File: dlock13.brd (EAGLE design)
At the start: 100 x 80 mm, 18 parts, among them IC2 7805T, Q1 IRLZ44Z, Q2 IRLZ44Z

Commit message: Updated.
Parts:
- removed R12: 4.7k, rcl:0207/10
- R5: value 470 -> 4.7k
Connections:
- removed net N$6: Q2.S, R12.2
- net GND: now also Q2.S; no longer R12.1
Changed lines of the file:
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@@
 <element name="R10" library="resistor" package="0204/7" value="470" x="29.23" y="41.34" rot="MR90"/>
 <element name="Q2" library="transistor-power" package="TO220BH" value="IRLZ44Z" x="23.89" y="31.02" rot="MR270"/>
-<element name="R5" library="resistor" package="0204/7" value="470" x="32.77" y="40.82" rot="MR270"/>
-<element name="R12" library="rcl" package="0207/10" value="4.7k" x="67.25" y="20.23" rot="MR0"/>
+<element name="R5" library="resistor" package="0204/7" value="4.7k" x="32.77" y="40.82" rot="MR270"/>
 <element name="D4" library="diode" package="DO41-10" value="1N4004" x="39.25" y="17.8" rot="MR0"/>
 <element name="JP1" library="pinhead" package="1X02" value="" x="26.66" y="4.53" rot="MR0"/>
@@
 <contactref element="C2" pad="2"/>
 <contactref element="C1" pad="2"/>
-<contactref element="R12" pad="1"/>
 <contactref element="JP1" pad="2"/>
 <contactref element="JP2" pad="2"/>
@@
 <contactref element="J3" pad="2"/>
 <contactref element="Q1" pad="S"/>
-<wire x1="5.06" y1="32.95" x2="27.86" y2="17.99" width="0" layer="19" extent="1-1"/>
-<wire x1="27.22" y1="68.24" x2="5.06" y2="32.95" width="0" layer="19" extent="1-1"/>
-<wire x1="7.97" y1="6.43" x2="5.06" y2="32.95" width="0" layer="19" extent="1-1"/>
-<wire x1="12.77" y1="3.43" x2="7.97" y2="6.43" width="0" layer="19" extent="1-1"/>
-<wire x1="72.33" y1="20.23" x2="27.86" y2="17.99" width="0" layer="19" extent="1-1"/>
-<wire x1="25.39" y1="4.53" x2="72.33" y2="20.23" width="0" layer="19" extent="1-1"/>
+<contactref element="Q2" pad="S"/>
+<wire x1="38.88" y1="40.61" x2="27.22" y2="68.24" width="0" layer="19" extent="1-1"/>
+<wire x1="30.24" y1="28.48" x2="38.88" y2="40.61" width="0" layer="19" extent="1-1"/>
+<wire x1="27.86" y1="17.99" x2="30.24" y2="28.48" width="0" layer="19" extent="1-1"/>
+<wire x1="35.36" y1="7.74" x2="27.86" y2="17.99" width="0" layer="19" extent="1-1"/>
+<wire x1="42.39" y1="7.64" x2="35.36" y2="7.74" width="0" layer="19" extent="1-1"/>
+<wire x1="25.39" y1="4.53" x2="35.36" y2="7.74" width="0" layer="19" extent="1-1"/>
 <wire x1="19.04" y1="4.53" x2="25.39" y2="4.53" width="0" layer="19" extent="1-1"/>
-<wire x1="42.39" y1="7.64" x2="25.39" y2="4.53" width="0" layer="19" extent="1-1"/>
-<wire x1="35.36" y1="7.74" x2="42.39" y2="7.64" width="0" layer="19" extent="1-1"/>
-<wire x1="38.88" y1="40.61" x2="19.04" y2="4.53" width="0" layer="19" extent="1-1"/>
+<wire x1="12.77" y1="3.43" x2="19.04" y2="4.53" width="0" layer="19" extent="1-1"/>
+<wire x1="7.97" y1="6.43" x2="12.77" y2="3.43" width="0" layer="19" extent="1-1"/>
+<wire x1="5.06" y1="32.95" x2="30.24" y2="28.48" width="0" layer="19" extent="1-1"/>
 </signal>
 <signal name="VCC">
@@
 <wire x1="29.23" y1="45.15" x2="22.14" y2="68.24" width="0" layer="19" extent="1-1"/>
 </signal>
-<signal name="N$6">
-<contactref element="R12" pad="2"/>
-<contactref element="Q2" pad="S"/>
-<wire x1="30.24" y1="28.48" x2="62.17" y2="20.23" width="0" layer="19" extent="1-1"/>
-</signal>
 <signal name="N$7">

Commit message: Add vidarkr's changes. Produced and In use.
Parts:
- removed SV1: (no value), con-ml:ML26
- added C3: (no value), rcl:E1,8-4
- added D1: 1N4004DO41-10LARGEPADS, diode:DO41-10
- added PICONNECTOR: RASPBERRY-PI, RaspberryPi:RASPBERRY-PI_REV1
- D4: value 1N4004 -> 1N4004DO41-10LARGEPADS
- R10, R5: device resistor:0204/7 -> rcl:0207/10
- moved R2 50.3 mm to (22.9, 20.3), flipped to the top, turned to 90 degrees
- moved LED1 47.0 mm to (68.6, 20.3), flipped to the top, turned to 90 degrees
- moved SV2 43.8 mm to (3.81, 35.6), flipped to the top
- moved Q1 40.6 mm to (56.0, 36.0), flipped to the top, turned to 0 degrees
- moved R1 39.5 mm to (26.7, 20.3), flipped to the top, turned to 90 degrees
- moved C2 36.7 mm to (2.54, 25.4), flipped to the top
- moved R3 32.9 mm to (64.8, 25.4), flipped to the top, turned to 0 degrees
- moved D4 25.1 mm to (20.3, 34.3), flipped to the top, turned to 90 degrees
- moved R10 22.9 mm to (45.7, 25.4), flipped to the top, turned to 0 degrees
- moved C1 22.8 mm to (43.2, 30.5), flipped to the top, turned to 90 degrees
- moved IC2 18.6 mm to (13.0, 36.0), flipped to the top, turned to 0 degrees
- moved Q2 14.3 mm to (35.6, 39.4), flipped to the top
- moved JP2 10.8 mm to (19.1, 15.2), flipped to the top, turned to 180 degrees
- moved JP1 9.37 mm to (20.3, 11.4), flipped to the top, turned to 180 degrees
- moved R5 8.64 mm to (24.1, 40.6), flipped to the top, turned to 90 degrees
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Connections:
- removed net N$1: R5.1, SV1.22
- removed net N$12: JP2.1, SV1.15
- removed net N$8: JP1.1, R1.1, SV1.16
- removed net N$9: LED1.A, SV1.26
- new net GPI10_OUTERDOOR: PICONNECTOR.19, R5.1
- new net GPIO11_INNERDOOR: PICONNECTOR.23, R10.1
- new net GPIO17_J1: JP1.1, PICONNECTOR.11, R1.1
- new net GPIO22_J2: JP2.1, PICONNECTOR.15, R2.1
- net +12V: now also D1.C
- net +3V3: now also PICONNECTOR.1; no longer SV1.1
- net GND: now also C3.-, PICONNECTOR.25, PICONNECTOR.9; no longer SV1.25
- net N$13: now also LED1.A, PICONNECTOR.26; no longer Q1.D, SV2.1
- net N$2: now also D1.A, Q1.D, SV2.1; no longer R10.1, SV1.18
- net VCC: now also C3.+, PICONNECTOR.2, PICONNECTOR.4; no longer SV1.2
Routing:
- net VCC: track 0.00 -> 88.2 mm, vias 0 -> 6
- net N$2: track 0.00 -> 77.9 mm
- net +12V: track 0.00 -> 55.9 mm
- net N$13: track 0.00 -> 51.0 mm
- net +3V3: track 0.00 -> 44.5 mm, vias 0 -> 2
- net GPI10_OUTERDOOR: track 0.00 -> 38.2 mm
- net GPIO22_J2: track 0.00 -> 35.0 mm
- net N$14: track 0.00 -> 29.0 mm
- net GPIO11_INNERDOOR: track 0.00 -> 27.2 mm
- net GPIO17_J1: track 0.00 -> 18.6 mm
- net N$7: track 0.00 -> 6.35 mm
- net N$4: track 0.00 -> 5.70 mm
- net N$11: track 0.00 -> 4.34 mm
- net N$15: track 0.00 -> 2.84 mm
- net N$9: track 0.00 -> 2.00 mm
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- added copper zone on layer 16, net GND
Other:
- board size 100 x 80 mm -> 72 x 51 mm

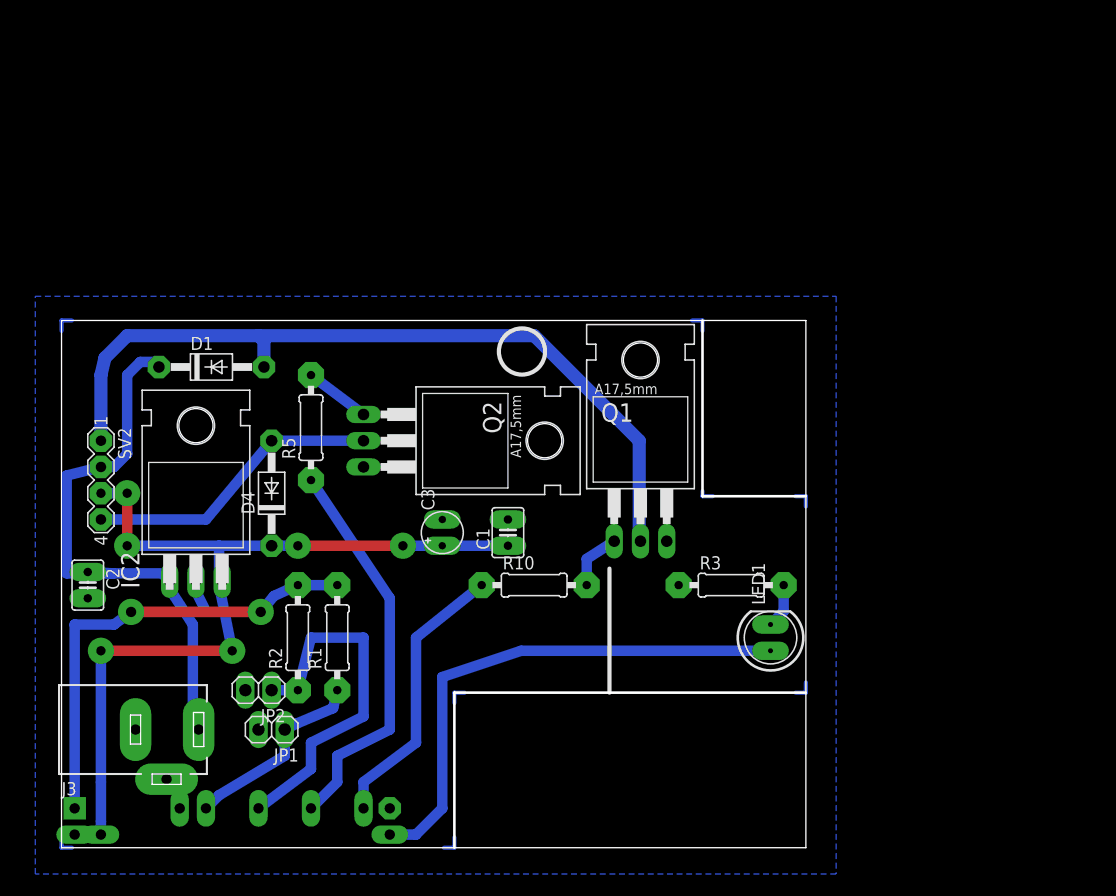
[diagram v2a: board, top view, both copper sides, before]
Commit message: Update dimension to follow board edge
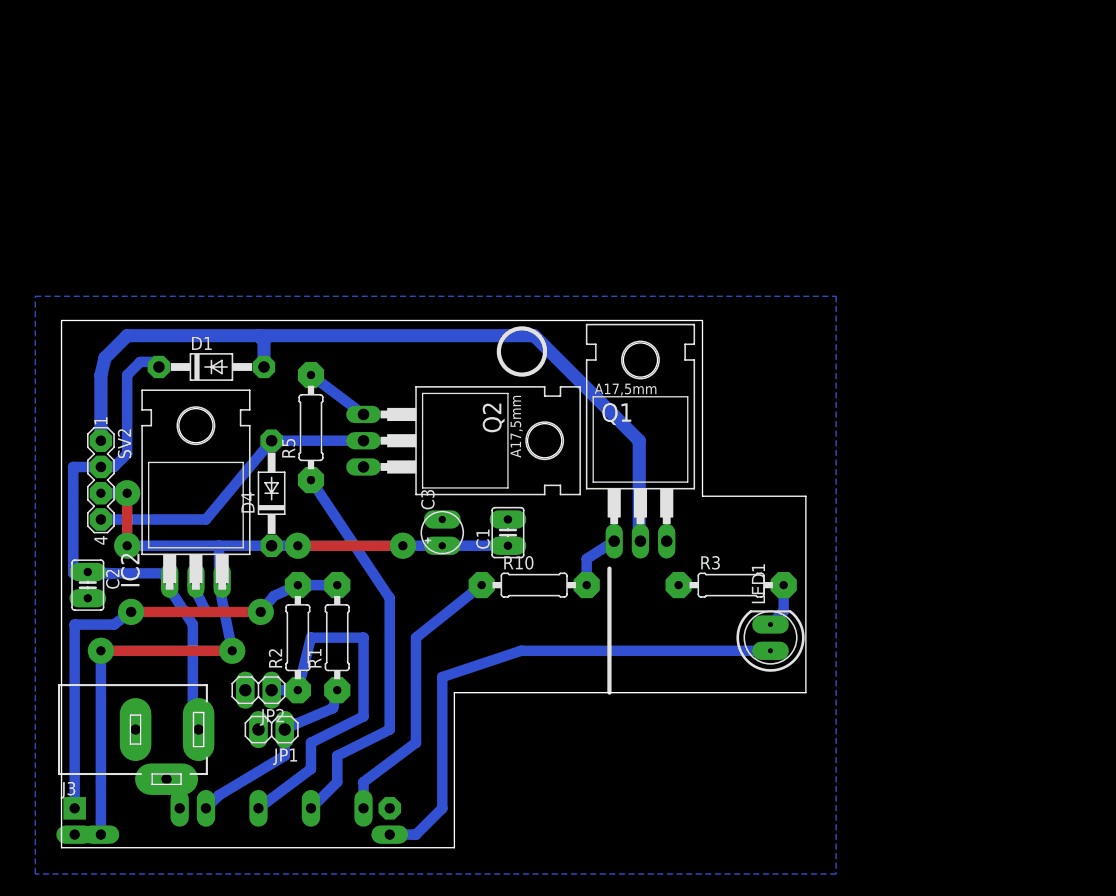
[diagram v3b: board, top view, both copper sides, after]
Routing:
- net N$9: track 2.00 -> 0.00 mm
- net N$8: track 2.00 -> 0.00 mm
- net N$6: track 2.00 -> 0.00 mm
- net N$5: track 2.00 -> 0.00 mm
- net N$3: track 2.00 -> 0.00 mm
- net N$12: track 2.00 -> 0.00 mm
- net N$1: track 2.00 -> 0.00 mm
- net N$10: track 1.50 -> 0.00 mm
- net +12V: track 55.9 -> 55.4 mm
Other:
- outline, holes or cut-outs redrawn
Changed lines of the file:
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@@
 <?xml version="1.0" encoding="utf-8"?>
 <!DOCTYPE eagle SYSTEM "eagle.dtd">
-<eagle version="6.4">
+<eagle version="7.5.0">
 <drawing>
 <settings>
@@
 <layer number="17" name="Pads" color="2" fill="1" visible="yes" active="yes"/>
 <layer number="18" name="Vias" color="2" fill="1" visible="yes" active="yes"/>
-<layer number="19" name="Unrouted" color="6" fill="1" visible="no" active="yes"/>
+<layer number="19" name="Unrouted" color="6" fill="1" visible="yes" active="yes"/>
 <layer number="20" name="Dimension" color="15" fill="1" visible="yes" active="yes"/>
 <layer number="21" name="tPlace" color="7" fill="1" visible="yes" active="yes"/>
@@
 <board>
 <plain>
-<wire x1="38" y1="0" x2="72" y2="0" width="0" layer="20"/>
-<wire x1="72" y1="0" x2="72" y2="15" width="0" layer="20"/>
 <wire x1="72" y1="15" x2="72" y2="34" width="0" layer="20"/>
-<wire x1="72" y1="34" x2="72" y2="51" width="0" layer="20"/>
-<wire x1="72" y1="51" x2="62" y2="51" width="0" layer="20"/>
 <wire x1="62" y1="51" x2="0" y2="51" width="0" layer="20"/>
 <wire x1="0" y1="51" x2="0" y2="0" width="0" layer="20"/>
 <circle x="44.54" y="48" radius="2.236065625" width="0.4064" layer="21"/>
-<wire x1="62" y1="51" x2="62" y2="34" width="0.254" layer="20"/>
-<wire x1="62" y1="34" x2="72" y2="34" width="0.254" layer="20"/>
-<wire x1="38" y1="0" x2="38" y2="15" width="0.254" layer="20"/>
-<wire x1="38" y1="15" x2="72" y2="15" width="0.254" layer="20"/>
+<wire x1="62" y1="51" x2="62" y2="34" width="0" layer="20"/>
+<wire x1="62" y1="34" x2="72" y2="34" width="0" layer="20"/>
+<wire x1="38" y1="0" x2="38" y2="15" width="0" layer="20"/>
+<wire x1="38" y1="15" x2="72" y2="15" width="0" layer="20"/>
 <wire x1="53" y1="27" x2="53" y2="15" width="0.4064" layer="21"/>
 <circle x="13" y="40.826" radius="0.925" width="1.551" layer="116"/>
@@
 <pass name="Default">
 <param name="RoutingGrid" value="50mil"/>
+<param name="AutoGrid" value="1"/>
+<param name="Efforts" value="0"/>
+<param name="TopRouterVariant" value="1"/>
 <param name="tpViaShape" value="round"/>
 <param name="PrefDir.1" value="|"/>
@@
 <wire x1="9.62" y1="26.54" x2="10.242034375" y2="25.36255" width="0.6096" layer="16"/>
 <wire x1="10.242034375" y1="25.36255" x2="10.46" y2="25.84" width="0.6096" layer="16"/>
-<wire x1="3.81" y1="36.83" x2="0.5" y2="36" width="1.016" layer="16"/>
-<wire x1="0.5" y1="36" x2="0.5" y2="26.54" width="1.016" layer="16"/>
-<wire x1="0.5" y1="26.54" x2="5" y2="26.54" width="1.016" layer="16"/>
+<wire x1="1.135" y1="26.54" x2="1.135" y2="36.83" width="1.016" layer="16"/>
+<wire x1="1.135" y1="36.83" x2="3.81" y2="36.83" width="1.016" layer="16"/>
+<wire x1="1.135" y1="26.54" x2="5" y2="26.54" width="1.016" layer="16"/>
 <contactref element="D1" pad="C"/>
 <wire x1="2.54" y1="26.67" x2="5" y2="26.54" width="1.016" layer="16"/>
@@
 <wire x1="19.58" y1="49" x2="19.05" y2="49.53" width="1.27" layer="16"/>
 </signal>
-<signal name="N$1">
-<wire x1="1" y1="51" x2="0" y2="51" width="0.4064" layer="16"/>
-<wire x1="0" y1="51" x2="0" y2="50" width="0.4064" layer="16"/>
-</signal>
-<signal name="N$3">
-<wire x1="0" y1="1" x2="0" y2="0" width="0.4064" layer="16"/>
-<wire x1="0" y1="0" x2="1" y2="0" width="0.4064" layer="16"/>
-</signal>
-<signal name="N$5">
-<wire x1="37" y1="0" x2="38" y2="0" width="0.4064" layer="16"/>
-<wire x1="38" y1="0" x2="38" y2="1" width="0.4064" layer="16"/>
-</signal>
-<signal name="N$6">
-<wire x1="38" y1="14" x2="38" y2="15" width="0.4064" layer="16"/>
-<wire x1="38" y1="15" x2="39" y2="15" width="0.4064" layer="16"/>
-</signal>
-<signal name="N$8">
-<wire x1="71" y1="15" x2="72" y2="15" width="0.4064" layer="16"/>
-<wire x1="72" y1="15" x2="72" y2="16" width="0.4064" layer="16"/>
-</signal>
-<signal name="N$9">
-<wire x1="71" y1="34" x2="72" y2="34" width="0.4064" layer="16"/>
-<wire x1="72" y1="34" x2="72" y2="33" width="0.4064" layer="16"/>
-</signal>
-<signal name="N$10">
-<wire x1="63" y1="34" x2="62" y2="34" width="0.4064" layer="16"/>
-<wire x1="62" y1="34" x2="62" y2="34.5" width="0.4064" layer="16"/>
-</signal>
-<signal name="N$12">
-<wire x1="61" y1="51" x2="62" y2="51" width="0.4064" layer="16"/>
-<wire x1="62" y1="51" x2="62" y2="50" width="0.4064" layer="16"/>
-</signal>
 <signal name="N$13">
